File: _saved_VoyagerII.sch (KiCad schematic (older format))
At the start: 5 parts, among them U1 ATXMEGA32A4U-AU

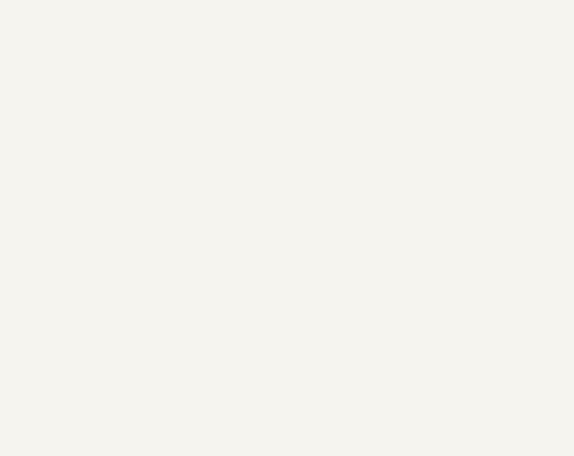
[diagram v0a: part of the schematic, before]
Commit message: Begin building schematic, bit by bit
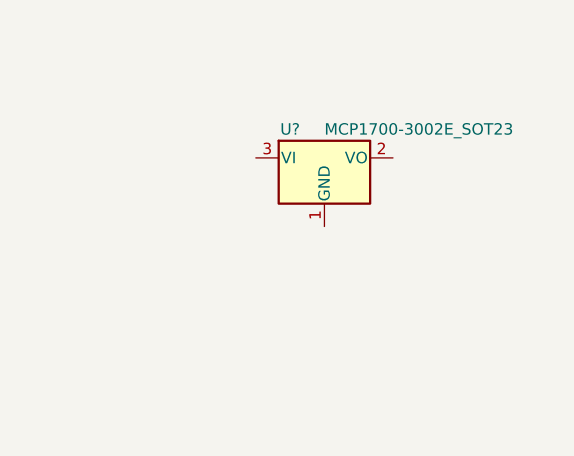
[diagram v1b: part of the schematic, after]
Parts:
- added U?: MCP1700-3002E_SOT23, TO_SOT_Packages_SMD:SOT-23, symbol MCP1700-3002E_SOT23
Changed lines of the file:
@@
+	1    0    0    -1
+$EndComp
+$Comp
+L MCP1700-3002E_SOT23 U?
+U 1 1 5A6246D3
+P 3950 1175
+F 0 "U?" H 3800 1300 50  0000 C CNN
+F 1 "MCP1700-3002E_SOT23" H 3950 1300 50  0000 L CNN
+F 2 "TO_SOT_Packages_SMD:SOT-23" H 3950 1400 50  0001 C CNN
+F 3 "" H 3950 1175 50  0001 C CNN
+	1    3950 1175
 	1    0    0    -1
 $EndComp
